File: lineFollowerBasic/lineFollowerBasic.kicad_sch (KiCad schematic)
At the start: 0 parts

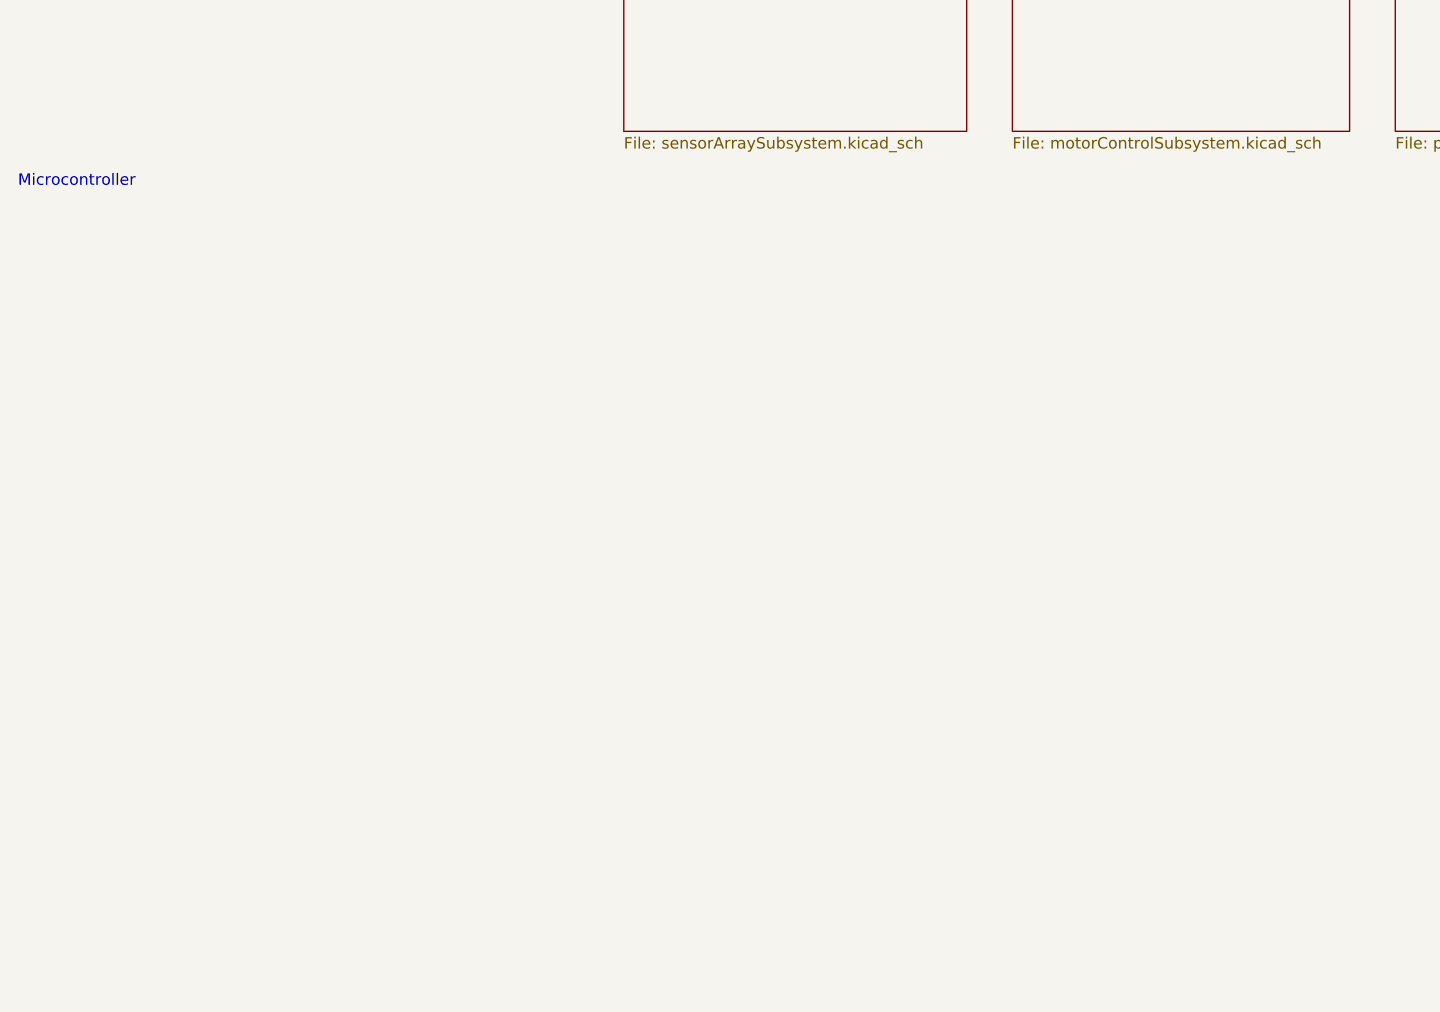
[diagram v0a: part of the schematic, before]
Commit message: Basic changes to MCU pins
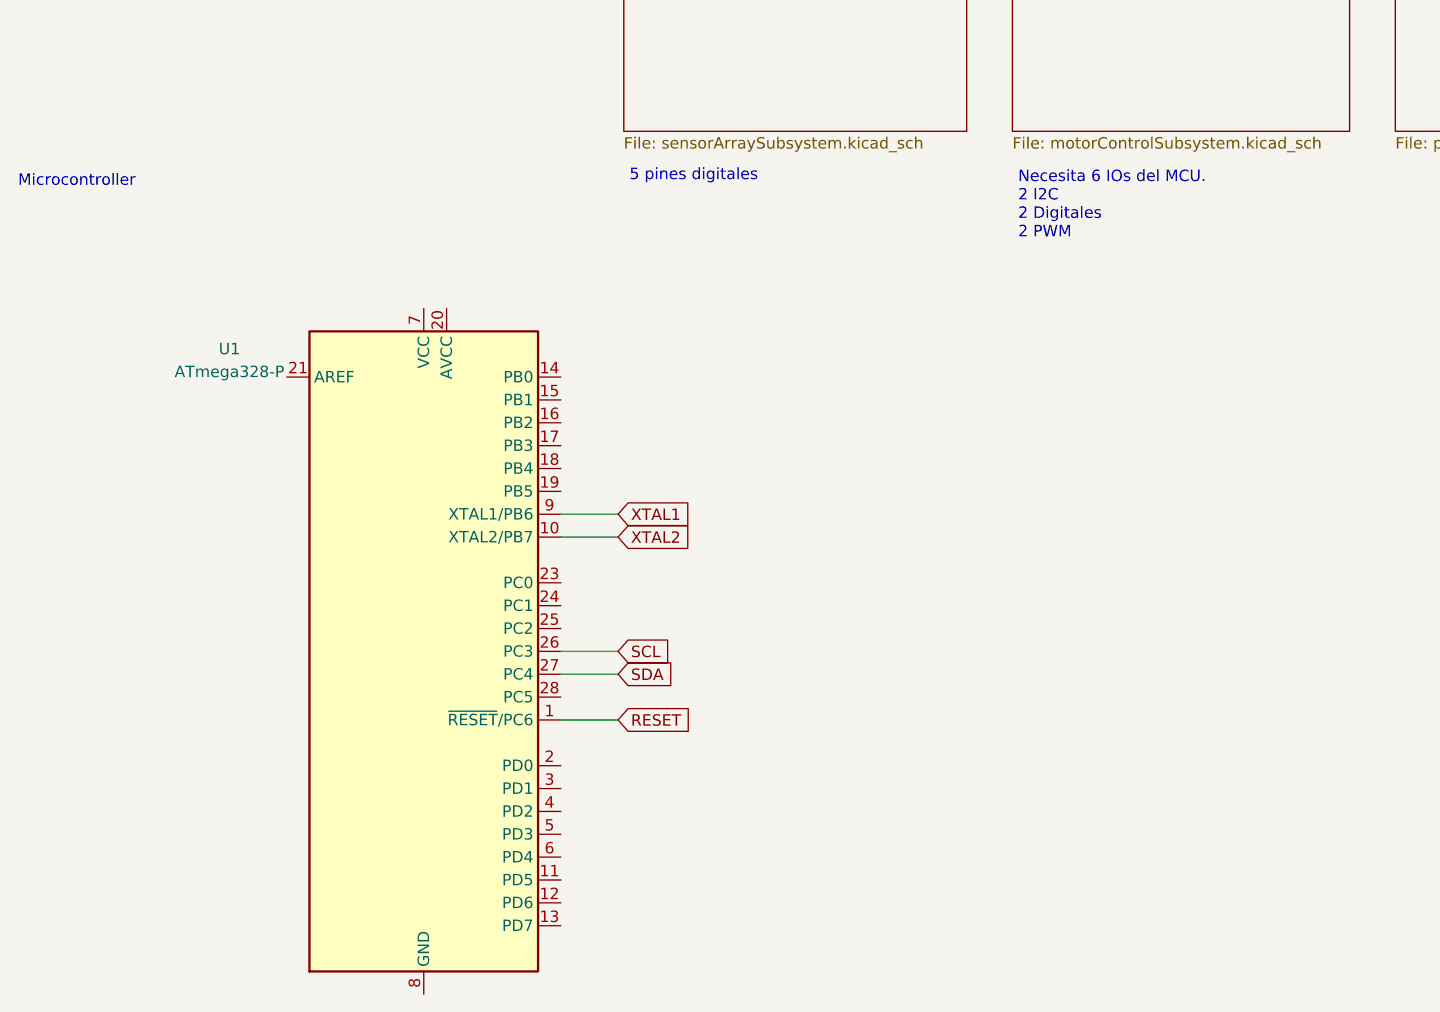
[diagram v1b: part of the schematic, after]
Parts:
- added U1: ATmega328-P, Package_DIP:DIP-28_W7.62mm, symbol MCU_Microchip_ATmega:ATmega328-P
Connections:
- new net: U1.22 (GND), U1.8 (GND)
- new net RESET: U1.1 (~{RESET}/PC6)
- new net SCL: U1.26 (PC3)
- new net SDA: U1.27 (PC4)
- new net XTAL1: U1.9 (XTAL1/PB6)
- new net XTAL2: U1.10 (XTAL2/PB7)
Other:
- note added: "5 pines digitales"
- note added: "Necesita 6 IOs del MCU. 2 I2C 2 Digitales 2 PWM"
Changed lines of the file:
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@@
 (kicad_sch (version 20230121) (generator eeschema)
   (paper "A4")
+  (wire (pts (xy 91.44 146.685) (xy 97.79 146.685))
+    (stroke (width 0) (type default))
+  )
+  (wire (pts (xy 91.44 141.605) (xy 97.79 141.605))
+    (stroke (width 0) (type default))
+  )
+  (wire (pts (xy 91.44 126.365) (xy 97.79 126.365))
+    (stroke (width 0) (type default))
+  )
+  (wire (pts (xy 91.44 123.825) (xy 97.79 123.825))
+    (stroke (width 0) (type default))
+  )
+  (wire (pts (xy 91.44 139.065) (xy 97.79 139.065))
+    (stroke (width 0) (type default))
+  )
   (text "Microcontroller\n" (at 31.115 87.63 0)
     (effects (font (size 1.27 1.27)) (justify left bottom))
   )
+  (text "5 pines digitales" (at 99.06 86.995 0)
+    (effects (font (size 1.27 1.27)) (justify left bottom))
+  )
+  (text "Necesita 6 IOs del MCU. \n2 I2C\n2 Digitales\n2 PWM" (at 142.24 93.345 0)
+    (effects (font (size 1.27 1.27)) (justify left bottom))
+  )
+  (global_label "XTAL2" (shape input) (at 97.79 126.365 0) (fields_autoplaced)
+    (effects (font (size 1.27 1.27)) (justify left))
+    (property "Intersheetrefs" "${INTERSHEET_REFS}" (at 106.1991 126.365 0)
+      (effects (font (size 1.27 1.27)) (justify left) hide)
+    )
+  )
+  (global_label "XTAL1" (shape input) (at 97.79 123.825 0) (fields_autoplaced)
+    (effects (font (size 1.27 1.27)) (justify left))
+    (property "Intersheetrefs" "${INTERSHEET_REFS}" (at 106.1991 123.825 0)
+      (effects (font (size 1.27 1.27)) (justify left) hide)
+    )
+  )
+  (global_label "SDA" (shape input) (at 97.79 141.605 0) (fields_autoplaced)
+    (effects (font (size 1.27 1.27)) (justify left))
+    (property "Intersheetrefs" "${INTERSHEET_REFS}" (at 104.2639 141.605 0)
+      (effects (font (size 1.27 1.27)) (justify left) hide)
+    )
+  )
+  (global_label "RESET" (shape input) (at 97.79 146.685 0) (fields_autoplaced)
+    (effects (font (size 1.27 1.27)) (justify left))
+    (property "Intersheetrefs" "${INTERSHEET_REFS}" (at 106.4409 146.685 0)
+      (effects (font (size 1.27 1.27)) (justify left) hide)
+    )
+  )
+  (global_label "SCL" (shape input) (at 97.79 139.065 0) (fields_autoplaced)
+    (effects (font (size 1.27 1.27)) (justify left))
+    (property "Intersheetrefs" "${INTERSHEET_REFS}" (at 104.2034 139.065 0)
+      (effects (font (size 1.27 1.27)) (justify left) hide)
+    )
+  )
+  (symbol (lib_id "MCU_Microchip_ATmega:ATmega328-P") (at 76.2 139.065 0) (unit 1)
+    (in_bom yes) (on_board yes) (dnp no) (fields_autoplaced)
+    (property "Reference" "U1" (at 54.61 105.4609 0)
+      (effects (font (size 1.27 1.27)))
+    )
+    (property "Value" "ATmega328-P" (at 54.61 108.0009 0)
+      (effects (font (size 1.27 1.27)))
+    )
+    (property "Footprint" "Package_DIP:DIP-28_W7.62mm" (at 76.2 139.065 0)
+      (effects (font (size 1.27 1.27) italic) hide)
+    )
+    (property "Datasheet" "http://ww1.microchip.com/downloads/en/DeviceDoc/ATmega328_P%20AVR%20MCU%20with%20picoPower%20Technology%20Data%20Sheet%2040001984A.pdf" (at 76.2 139.065 0)
+      (effects (font (size 1.27 1.27)) hide)
+    )
+    (pin "1")
+    (pin "10")
+    (pin "11")
+    (pin "12")
+    (pin "13")
+    (pin "14")
+    (pin "15")
+    (pin "16")
+    (pin "17")
+    (pin "18")
+    (pin "19")
+    (pin "2")
+    (pin "20")
+    (pin "21")
+    (pin "22")
+    (pin "23")
+    (pin "24")
+    (pin "25")
+    (pin "26")
+    (pin "27")
+    (pin "28")
+    (pin "3")
+    (pin "4")
+    (pin "5")
+    (pin "6")
+    (pin "7")
+    (pin "8")
+    (pin "9")
+    (instances
+      (project "lineFollowerBasic"
+        (path "/751730cf-cec6-4b73-8a36-3b45eebd4e7c"
+          (reference "U1") (unit 1)
+        )
+      )
+    )
+  )
   (sheet (at 227.33 27.305) (size 38.735 53.975) (fields_autoplaced)

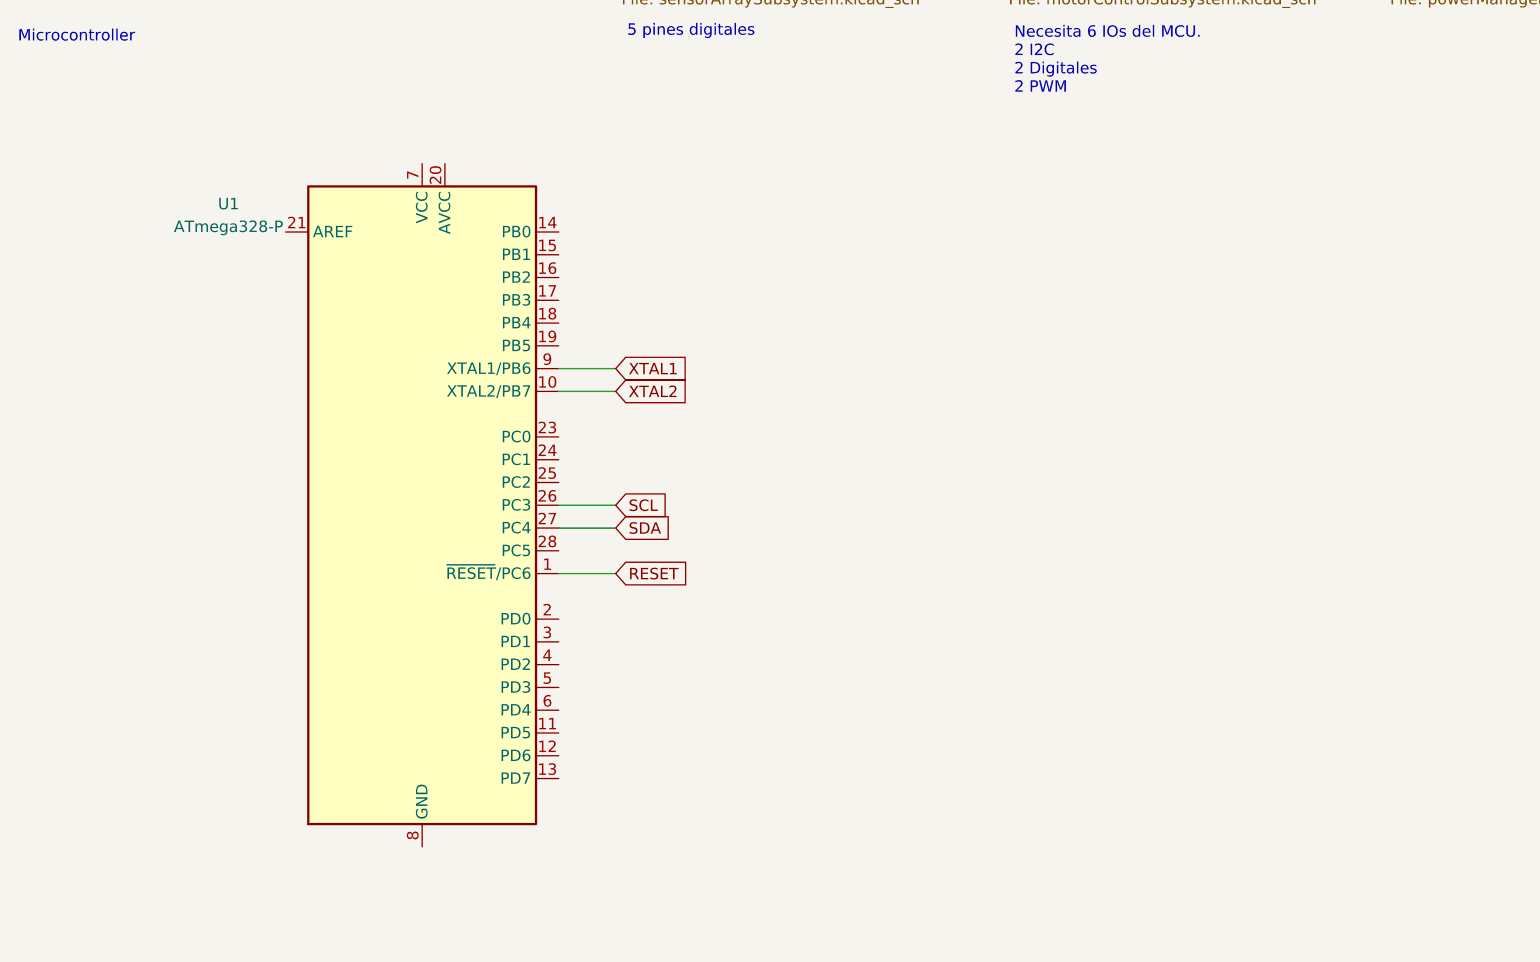
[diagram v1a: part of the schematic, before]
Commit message: Modified MCU Sch: added crystal, capacitors, FTDI conn, power symbols. Modified Power Module: added battery module, new symbol for converter, power symbols.
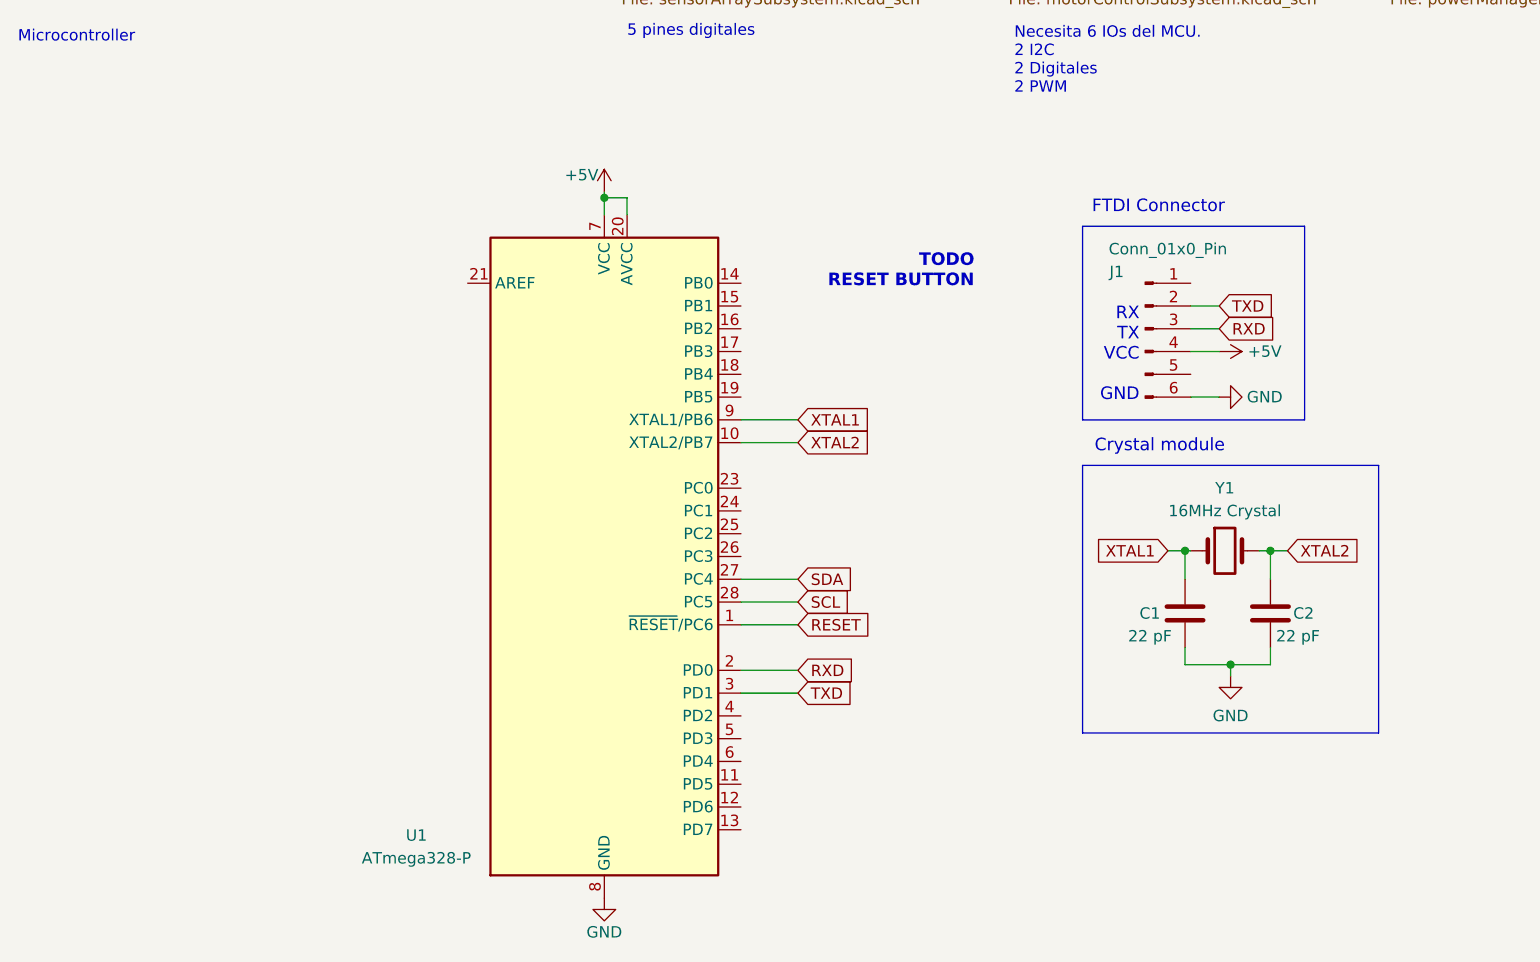
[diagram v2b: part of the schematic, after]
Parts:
- added C1, C2: 22 pF, symbol Device:C
- added J1: Conn_01x0_Pin, symbol Connector:Conn_01x06_Pin
- added Y1: 16MHz Crystal, symbol Device:Crystal
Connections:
- net SCL: now also U1.28 (PC5); no longer U1.26 (PC3)
- net XTAL1: now also C1.1, Y1.1
- net XTAL2: now also C2.1, Y1.2
- net RXD: now reaches U1.2 (PD0)
- net RXD: now also J1.3 (Pin_3)
- net +5V: now reaches U1.20 (AVCC)
- net +5V: now also U1.7 (VCC), J1.4 (Pin_4)
- net GND: now reaches U1.22 (GND), U1.8 (GND)
- net GND: now also C1.2, C2.2, J1.6 (Pin_6)
- net TXD: now reaches U1.3 (PD1)
- net TXD: now also J1.2 (Pin_2)
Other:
- note added: "Crystal module"
- note added: "FTDI Connector"
- note added: "RX TX VCC GND"
- note added: "TODO RESET BUTTON"
- moved on the sheet: U1

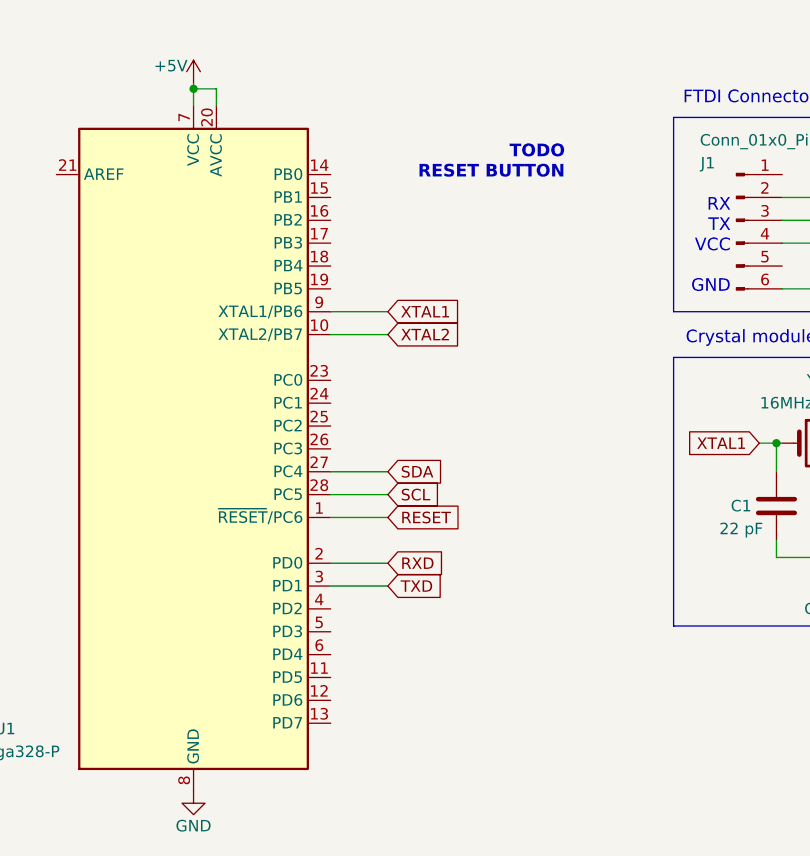
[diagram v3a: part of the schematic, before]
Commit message: Deleted extra ATMEGAs, added labels
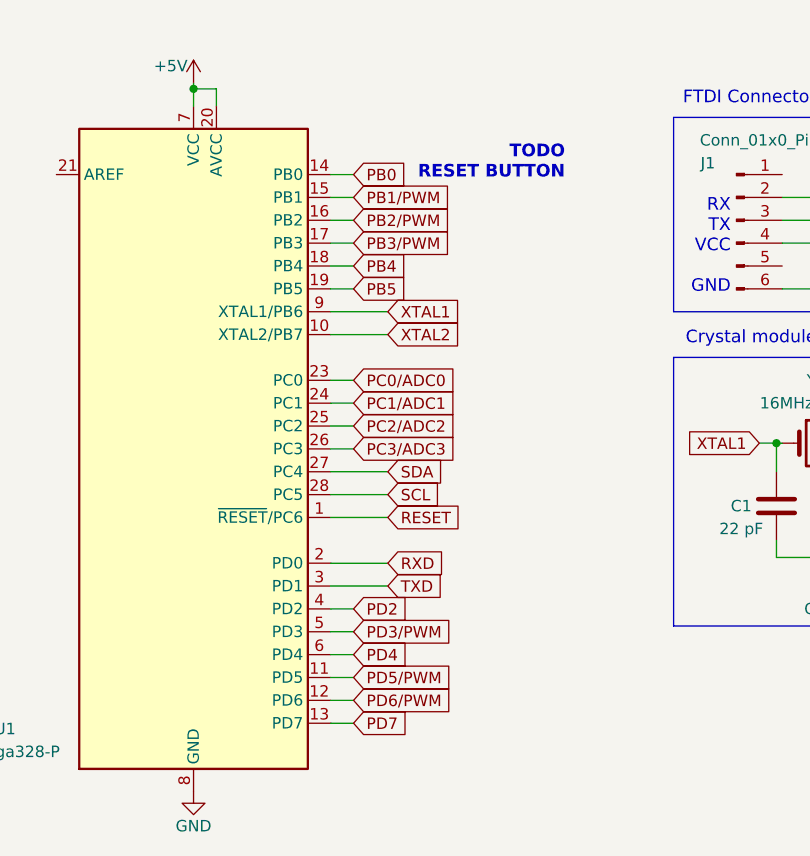
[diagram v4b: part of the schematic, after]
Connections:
- net PD5/PWM: now reaches U1.11 (PD5)
- net PD6/PWM: now reaches U1.12 (PD6)
- net PD7: now reaches U1.13 (PD7)
- net PB0: now reaches U1.14 (PB0)
- net PB1/PWM: now reaches U1.15 (PB1)
- net PB2/PWM: now reaches U1.16 (PB2)
- net PB3/PWM: now reaches U1.17 (PB3)
- net PB4: now reaches U1.18 (PB4)
- net PB5: now reaches U1.19 (PB5)
- net PC0/ADC0: now reaches U1.23 (PC0)
- net PC1/ADC1: now reaches U1.24 (PC1)
- net PC2/ADC2: now reaches U1.25 (PC2)
- net PC3/ADC3: now reaches U1.26 (PC3)
- net PD2: now reaches U1.4 (PD2)
- net PD3/PWM: now reaches U1.5 (PD3)
- net PD4: now reaches U1.6 (PD4)

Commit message: added reset button module
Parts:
- added R7: 10k, symbol Device:R
- added SW1: SW_Push, symbol Switch:SW_Push
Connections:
- net +5V: now also R7.1
- net GND: now also SW1.2
- net RESET: now also R7.2, SW1.1
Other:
- note added: "Reset Module"
